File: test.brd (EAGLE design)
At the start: 28.9 x 20.9 mm, 16 parts

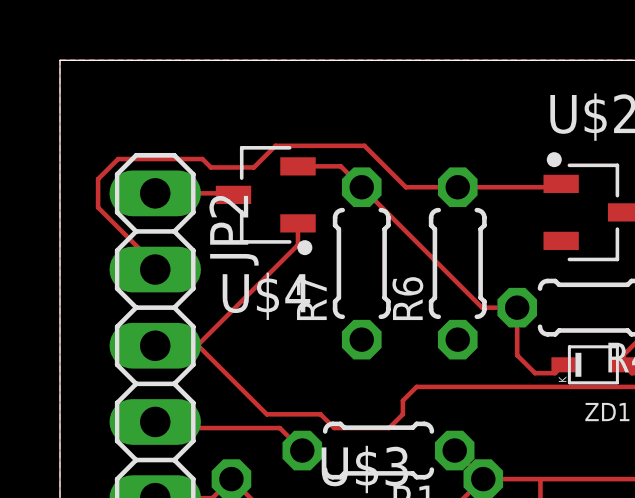
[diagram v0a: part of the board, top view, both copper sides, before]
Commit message: rearrainged devies and added a solder junction
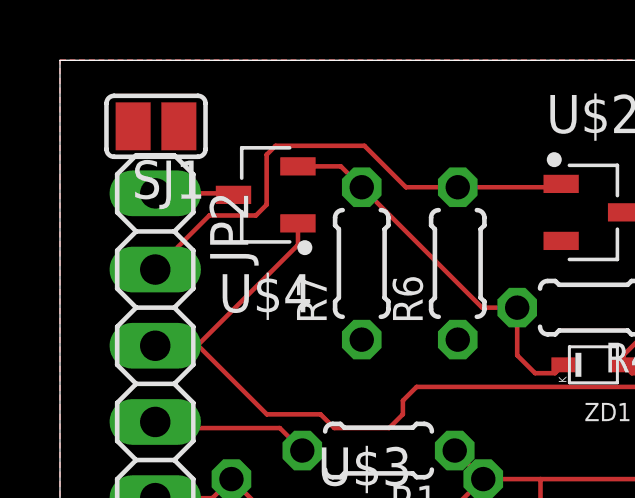
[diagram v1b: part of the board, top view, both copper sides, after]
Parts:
- added SJ1: (no value), jumper:SJ
- R3: value 105 -> 104
- U$3: value 2SK3072-TB-E -> IRLML6344TRPBFTR
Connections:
- net N$6: now also SJ1.1
- net VDD: now also SJ1.2
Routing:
- net N$5: track 20.5 -> 17.0 mm
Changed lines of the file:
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@@
 <layers>
 <layer number="1" name="Top" color="4" fill="1" visible="yes" active="yes"/>
+<layer number="2" name="Route2" color="1" fill="3" visible="no" active="no"/>
+<layer number="3" name="Route3" color="4" fill="3" visible="no" active="no"/>
+<layer number="4" name="Route4" color="1" fill="4" visible="no" active="no"/>
+<layer number="5" name="Route5" color="4" fill="4" visible="no" active="no"/>
+<layer number="6" name="Route6" color="1" fill="8" visible="no" active="no"/>
+<layer number="7" name="Route7" color="4" fill="8" visible="no" active="no"/>
+<layer number="8" name="Route8" color="1" fill="2" visible="no" active="no"/>
+<layer number="9" name="Route9" color="4" fill="2" visible="no" active="no"/>
+<layer number="10" name="Route10" color="1" fill="7" visible="no" active="no"/>
+<layer number="11" name="Route11" color="4" fill="7" visible="no" active="no"/>
+<layer number="12" name="Route12" color="1" fill="5" visible="no" active="no"/>
+<layer number="13" name="Route13" color="4" fill="5" visible="no" active="no"/>
+<layer number="14" name="Route14" color="1" fill="6" visible="no" active="no"/>
+<layer number="15" name="Route15" color="4" fill="6" visible="no" active="no"/>
 <layer number="16" name="Bottom" color="1" fill="1" visible="yes" active="yes"/>
 <layer number="17" name="Pads" color="2" fill="1" visible="yes" active="yes"/>
@@
 <attribute name="VALUE" x="16.4211" y="2.3114" size="0.9906" layer="27" ratio="10" rot="R90"/>
 </element>
-<element name="R3" library="rcl" library_urn="urn:adsk.eagle:library:334" package="0204/5" package3d_urn="urn:adsk.eagle:package:23488/1" value="105" x="21.9075" y="15.24" smashed="yes" rot="R270">
+<element name="R3" library="rcl" library_urn="urn:adsk.eagle:library:334" package="0204/5" package3d_urn="urn:adsk.eagle:package:23488/1" value="104" x="21.9075" y="15.24" smashed="yes" rot="R270">
 <attribute name="NAME" x="23.0759" y="17.2466" size="0.9906" layer="25" ratio="10" rot="R270"/>
 <attribute name="SPICEPREFIX" value="R" x="-11.1125" y="-1.27" size="1.778" layer="27" rot="R270" display="off"/>
@@
 <attribute name="VALUE" x="17.78" y="13.6714" size="1.27" layer="27" align="top-center"/>
 </element>
-<element name="U$3" library="Transistor-FET" library_urn="urn:adsk.eagle:library:11887002" package="SOT95P250X120-3" package3d_urn="urn:adsk.eagle:package:11886978/1" value="2SK3072-TB-E" x="10.16" y="4.1275" smashed="yes">
+<element name="U$3" library="Transistor-FET" library_urn="urn:adsk.eagle:library:11887002" package="SOT95P250X120-3" package3d_urn="urn:adsk.eagle:package:11886978/1" value="IRLML6344TRPBFTR" x="10.16" y="4.1275" smashed="yes">
 <attribute name="NAME" x="10.16" y="6.7711" size="1.27" layer="25" align="bottom-center"/>
 <attribute name="VALUE" x="10.16" y="1.9239" size="1.27" layer="27" align="top-center"/>
@@
 <attribute name="SPICEPREFIX" value="R" x="10.0584" y="14.1732" size="1.778" layer="27" rot="R90" display="off"/>
 <attribute name="VALUE" x="12.3698" y="12.0396" size="0.9906" layer="27" ratio="10" rot="R90"/>
+</element>
+<element name="SJ1" library="jumper" library_urn="urn:adsk.eagle:library:252" package="SJ" package3d_urn="urn:adsk.eagle:package:15471/1" value="" x="3.2004" y="18.7452" smashed="yes" rot="R180">
+<attribute name="NAME" x="4.8514" y="17.6022" size="1.27" layer="25" ratio="10" rot="R180"/>
+<attribute name="VALUE" x="2.8003" y="18.7452" size="0.02" layer="27" rot="R180"/>
 </element>
 </elements>
@@
 <wire x1="16.5937" y1="16.7132" x2="13.2588" y2="16.7132" width="0.1524" layer="1"/>
 <wire x1="11.5311625" y1="16.7132" x2="13.2588" y2="16.7132" width="0.1524" layer="1"/>
-<wire x1="1.27" y1="16.03655" x2="1.27" y2="16.98345" width="0.1524" layer="1"/>
-<wire x1="1.27" y1="16.98345" x2="1.93955" y2="17.653" width="0.1524" layer="1"/>
 <wire x1="3.175" y1="13.97" x2="3.175" y2="14.13155" width="0.1524" layer="1"/>
-<wire x1="3.175" y1="14.13155" x2="1.27" y2="16.03655" width="0.1524" layer="1"/>
-<wire x1="1.93955" y1="17.653" x2="4.7498" y2="17.653" width="0.1524" layer="1"/>
-<wire x1="4.7498" y1="17.653" x2="5.0292" y2="17.3736" width="0.1524" layer="1"/>
 <wire x1="7.1846375" y1="18.0948" x2="10.1495625" y2="18.0948" width="0.1524" layer="1"/>
 <wire x1="10.1495625" y1="18.0948" x2="11.5311625" y2="16.7132" width="0.1524" layer="1"/>
-<wire x1="5.0292" y1="17.3736" x2="6.4634375" y2="17.3736" width="0.1524" layer="1"/>
-<wire x1="6.4634375" y1="17.3736" x2="7.1846375" y2="18.0948" width="0.1524" layer="1"/>
+<wire x1="6.88931875" y1="17.79948125" x2="7.1846375" y2="18.0948" width="0.1524" layer="1"/>
+<wire x1="3.175" y1="13.97" x2="4.9786" y2="15.7736" width="0.1524" layer="1"/>
+<wire x1="4.9786" y1="15.7736" x2="6.5313625" y2="15.7736" width="0.1524" layer="1"/>
+<wire x1="6.5313625" y1="15.7736" x2="6.88931875" y2="16.13155625" width="0.1524" layer="1"/>
+<wire x1="6.88931875" y1="16.13155625" x2="6.88931875" y2="17.79948125" width="0.1524" layer="1"/>
 </signal>
 <signal name="N$7">
@@
 <wire x1="10.0584" y1="16.7132" x2="14.0716" y2="12.7" width="0.1524" layer="1"/>
 <wire x1="14.0716" y1="12.7" x2="15.24" y2="12.7" width="0.1524" layer="1"/>
+<contactref element="SJ1" pad="1"/>
+<wire x1="3.9624" y1="18.7452" x2="15.8369" y2="10.5156" width="0" layer="19" extent="1-1"/>
 </signal>
 <signal name="VDD">
@@
 <wire x1="3.175" y1="16.51" x2="5.7327" y2="16.51" width="0.1524" layer="1"/>
 <wire x1="5.7327" y1="16.51" x2="5.7835" y2="16.4592" width="0.1524" layer="1"/>
+<contactref element="SJ1" pad="2"/>
+<wire x1="2.4384" y1="18.7452" x2="3.175" y2="16.51" width="0" layer="19" extent="1-1"/>
 </signal>
 </signals>
